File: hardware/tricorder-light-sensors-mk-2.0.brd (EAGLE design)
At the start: 12.7 x 12.7 mm, 8 parts, among them U1 VEML6075, U2 APDS-9250

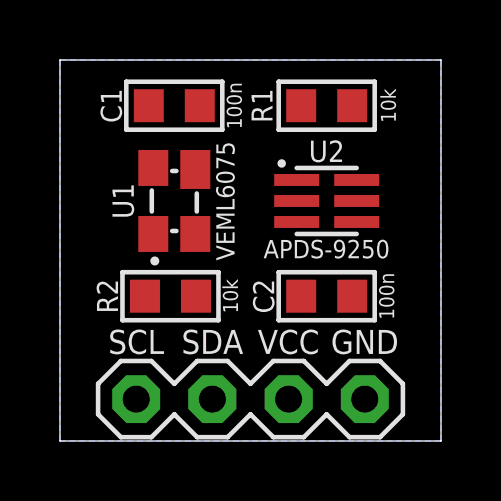
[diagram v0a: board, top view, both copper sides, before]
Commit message: swap apds9250 for tcs3400
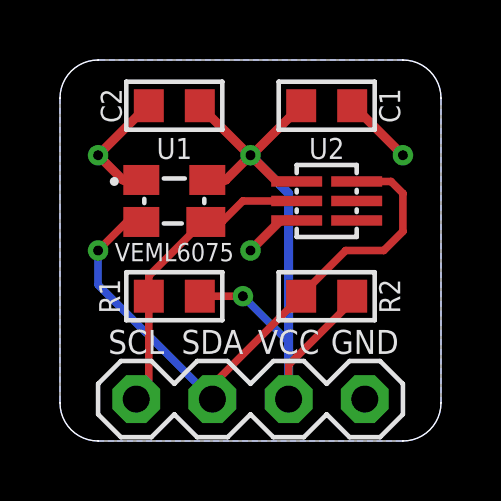
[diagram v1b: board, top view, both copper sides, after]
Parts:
- C1: value 100n -> 1u
- U2: value APDS-9250 -> TCS3400; device a_parts:APDS-9250-ALT -> a_parts:TCS3400_DFN6
- moved C2 8.13 mm to (3.81, 11.2), turned to 180 degrees
- moved R1 8.13 mm to (3.81, 4.83)
- moved R2 5.21 mm to (8.89, 4.83), turned to 180 degrees
- moved C1 5.08 mm to (8.89, 11.2)
- turned U1 to 0 degrees
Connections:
- net 3.3V: now also U2.1; no longer U2.3
- net GND: now also U2.3; no longer U2.6
- net SCL: now also U2.2; no longer U2.1
- net SDA: now also U2.6; no longer U2.2
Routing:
- net 3.3V: track 0.00 -> 25.2 mm, vias 0 -> 2
- net SDA: track 0.00 -> 20.3 mm, vias 0 -> 1
- net SCL: track 0.00 -> 10.2 mm
- net GND: track 0.00 -> 8.48 mm, vias 0 -> 3
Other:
- outline, holes or cut-outs redrawn
